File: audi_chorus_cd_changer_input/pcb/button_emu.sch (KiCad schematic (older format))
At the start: 7 parts, among them IC1 ATTINY85-P, P1 CONN_1, P2 CONN_1, P3 CONN_1, P4 CONN_1, P5 CONN_1

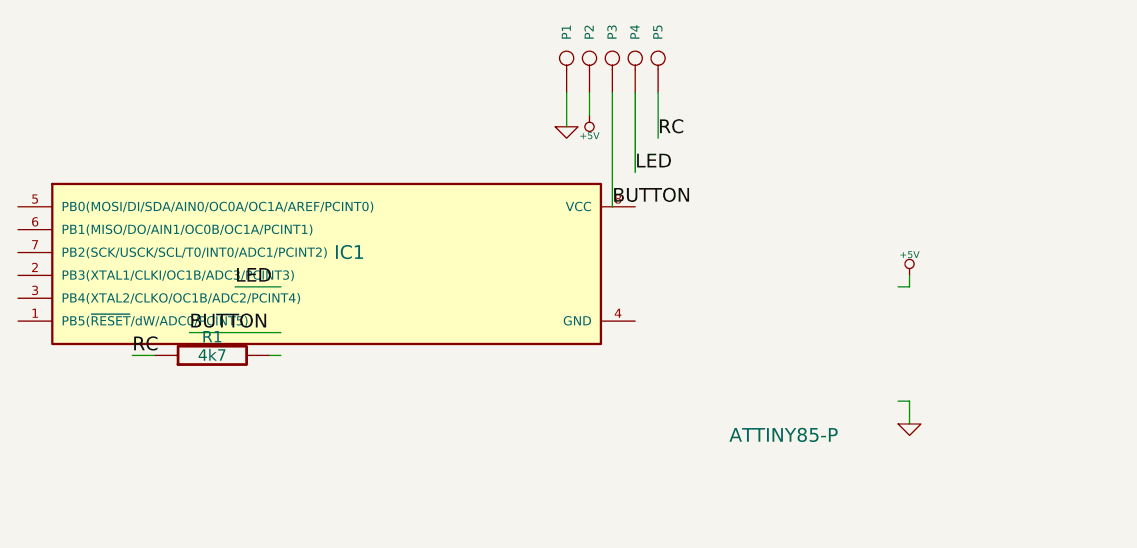
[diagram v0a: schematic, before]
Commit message: update audi chorus enable cd changer input pcb for new kicad version, soic 8 package with wide pads for handsoldering
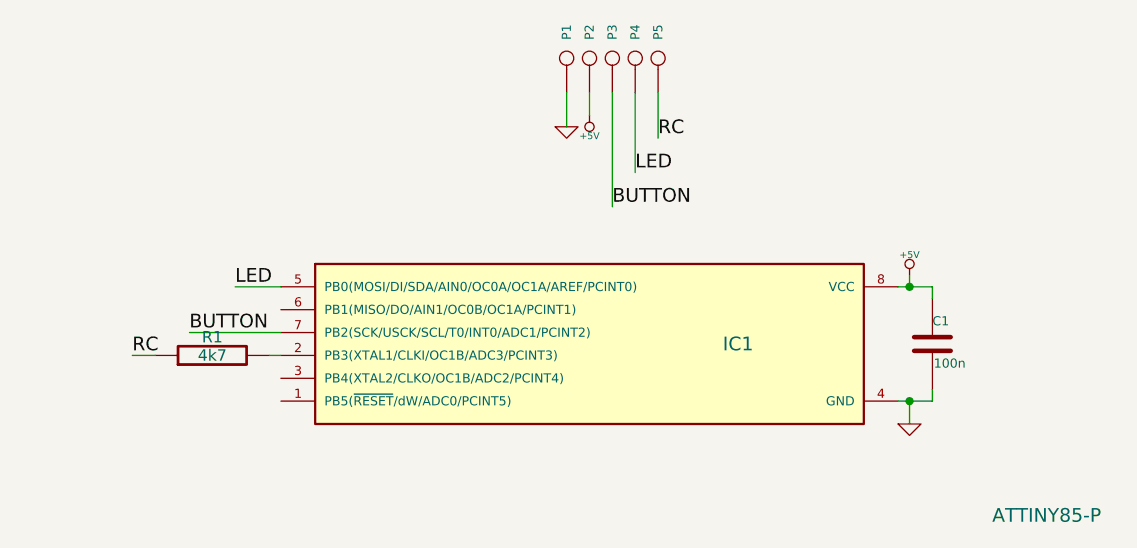
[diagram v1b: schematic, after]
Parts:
- added C1: 100n, symbol C
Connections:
- wire segments 13 -> 15
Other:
- moved on the sheet: IC1
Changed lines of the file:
@@
-EESchema Schematic File Version 2  date Wed 19 Feb 2014 05:22:19 PM CET
+EESchema Schematic File Version 2
 LIBS:power
 LIBS:device
@@
 LIBS:valves
 LIBS:button_emu-cache
-EELAYER 25  0
+EELAYER 25 0
 EELAYER END
-$Descr A4 11700 8267
+$Descr A4 11693 8268
 encoding utf-8
 Sheet 1 1
@@
 	5450 3700 5500 3700
 Wire Wire Line
-	8200 3400 8250 3400
+	8200 3400 8350 3400
 Wire Wire Line
 	8250 3400 8250 3350
 Wire Wire Line
-	8200 3900 8250 3900
+	8200 3900 8350 3900
 Wire Wire Line
 	8250 3900 8250 4000
@@
 F 0 "P5" H 7230 2400 40  0000 L CNN
 F 1 "CONN_1" H 7150 2455 30  0001 C CNN
+F 2 "" H 7150 2400 60  0001 C CNN
+F 3 "" H 7150 2400 60  0001 C CNN
 	1    7150 2400
 	0    -1   -1   0
@@
 F 0 "P4" H 7130 2400 40  0000 L CNN
 F 1 "CONN_1" H 7050 2455 30  0001 C CNN
+F 2 "" H 7050 2400 60  0001 C CNN
+F 3 "" H 7050 2400 60  0001 C CNN
 	1    7050 2400
 	0    -1   -1   0
@@
 F 0 "P3" H 7030 2400 40  0000 L CNN
 F 1 "CONN_1" H 6950 2455 30  0001 C CNN
+F 2 "" H 6950 2400 60  0001 C CNN
+F 3 "" H 6950 2400 60  0001 C CNN
 	1    6950 2400
 	0    -1   -1   0
@@
 F 0 "P2" H 6930 2400 40  0000 L CNN
 F 1 "CONN_1" H 6850 2455 30  0001 C CNN
+F 2 "" H 6850 2400 60  0001 C CNN
+F 3 "" H 6850 2400 60  0001 C CNN
 	1    6850 2400
 	0    -1   -1   0
@@
 F 0 "P1" H 6830 2400 40  0000 L CNN
 F 1 "CONN_1" H 6750 2455 30  0001 C CNN
+F 2 "" H 6750 2400 60  0001 C CNN
+F 3 "" H 6750 2400 60  0001 C CNN
 	1    6750 2400
 	0    -1   -1   0
@@
 F 0 "R1" V 5280 3700 50  0000 C CNN
 F 1 "4k7" V 5200 3700 50  0000 C CNN
+F 2 "" H 5200 3700 60  0001 C CNN
+F 3 "" H 5200 3700 60  0001 C CNN
 	1    5200 3700
 	0    -1   -1   0
@@
 RC
 $Comp
-L +5V #PWR3
+L +5V #PWR01
 U 1 1 53049D4F
 P 8250 3350
-F 0 "#PWR3" H 8250 3440 20  0001 C CNN
+F 0 "#PWR01" H 8250 3440 20  0001 C CNN
 F 1 "+5V" H 8250 3440 30  0000 C CNN
+F 2 "" H 8250 3350 60  0001 C CNN
+F 3 "" H 8250 3350 60  0001 C CNN
 	1    8250 3350
 	1    0    0    -1
 $EndComp
 $Comp
-L +5V #PWR2
+L +5V #PWR02
 U 1 1 53049D41
 P 6850 2650
-F 0 "#PWR2" H 6850 2740 20  0001 C CNN
+F 0 "#PWR02" H 6850 2740 20  0001 C CNN
 F 1 "+5V" H 6850 2740 30  0000 C CNN
+F 2 "" H 6850 2650 60  0001 C CNN
+F 3 "" H 6850 2650 60  0001 C CNN
 	1    6850 2650
 	-1   0    0    1
 $EndComp
 $Comp
-L GND #PWR4
+L GND #PWR03
 U 1 1 53049D2A
 P 8250 4000
-F 0 "#PWR4" H 8250 4000 30  0001 C CNN
+F 0 "#PWR03" H 8250 4000 30  0001 C CNN
 F 1 "GND" H 8250 3930 30  0001 C CNN
+F 2 "" H 8250 4000 60  0001 C CNN
+F 3 "" H 8250 4000 60  0001 C CNN
 	1    8250 4000
 	1    0    0    -1
 $EndComp
 $Comp
-L GND #PWR1
+L GND #PWR04
 U 1 1 53049D25
 P 6750 2700
-F 0 "#PWR1" H 6750 2700 30  0001 C CNN
+F 0 "#PWR04" H 6750 2700 30  0001 C CNN
 F 1 "GND" H 6750 2630 30  0001 C CNN
+F 2 "" H 6750 2700 60  0001 C CNN
+F 3 "" H 6750 2700 60  0001 C CNN
 	1    6750 2700
 	1    0    0    -1
@@
 L ATTINY85-P IC1
 U 1 1 53049CE1
-P 5700 3300
-F 0 "IC1" H 5800 3350 60  0000 C CNN
-F 1 "ATTINY85-P" H 7700 2550 60  0000 C CNN
-F 2 "DIP8" H 5800 2550 60  0001 C CNN
-	1    5700 3300
-	1    0    0    -1
-$EndComp
+P 6850 3650
+F 0 "IC1" H 7500 3650 60  0000 C CNN
+F 1 "ATTINY85-P" H 8850 2900 60  0000 C CNN
+F 2 "DIP8" H 6950 2900 60  0001 C CNN
+F 3 "" H 6850 3650 60  0001 C CNN
+	1    6850 3650
+	1    0    0    -1
+$EndComp
+$Comp
+L C C1
+U 1 1 54326E19
+P 8350 3650
+F 0 "C1" H 8350 3750 40  0000 L CNN
+F 1 "100n" H 8356 3565 40  0000 L CNN
+F 2 "" H 8388 3500 30  0000 C CNN
+F 3 "" H 8350 3650 60  0000 C CNN
+	1    8350 3650
+	1    0    0    -1
+$EndComp
+Wire Wire Line
+	8350 3400 8350 3450
+Connection ~ 8250 3400
+Wire Wire Line
+	8350 3900 8350 3850
+Connection ~ 8250 3900
 $EndSCHEMATC
